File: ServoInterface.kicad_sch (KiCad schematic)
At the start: 7 parts, among them J10 ServoInputSW, J11 ServoOut

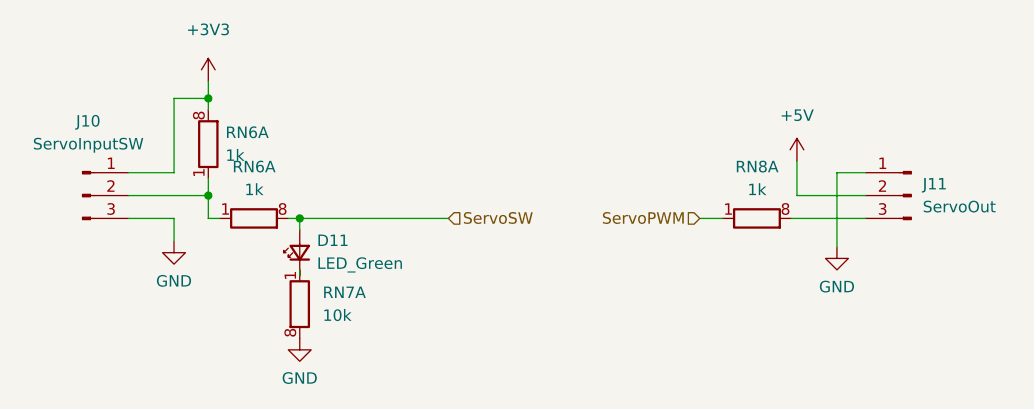
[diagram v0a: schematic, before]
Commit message: Silkscreen updates
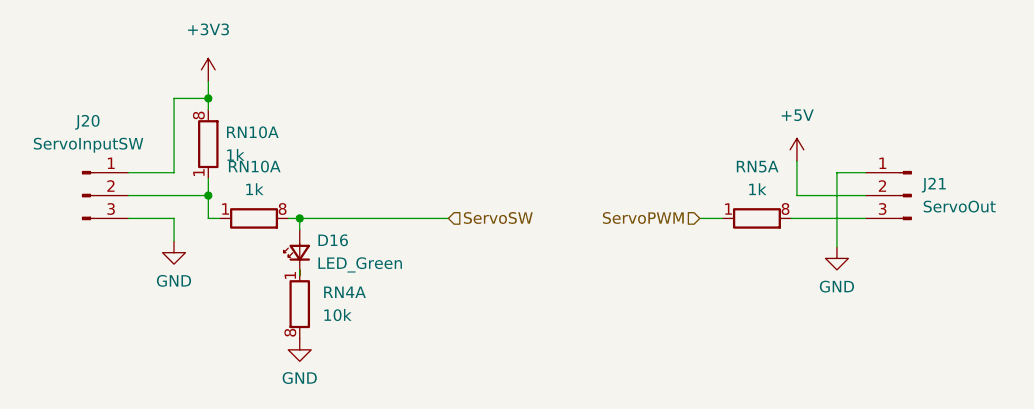
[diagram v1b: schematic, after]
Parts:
- renumbered D11 to D16, J10 to J20, J11 to J21, RN6 to RN10, RN7 to RN4, RN8 to RN5
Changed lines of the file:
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@@
   (symbol (lib_id "power:GND") (at 95.885 83.185 0)
     (in_bom yes) (on_board yes) (fields_autoplaced)
-    (property "Reference" "#PWR059" (id 0) (at 95.885 89.535 0)
+    (property "Reference" "#PWR061" (id 0) (at 95.885 89.535 0)
       (effects (font (size 1.27 1.27)) hide)
     )
@@
   (symbol (lib_id "Device:R_Pack04_Split") (at 160.655 80.645 270)
     (in_bom yes) (on_board yes) (fields_autoplaced)
-    (property "Reference" "RN8" (id 0) (at 160.655 74.93 90))
+    (property "Reference" "RN5" (id 0) (at 160.655 74.93 90))
     (property "Value" "1k" (id 1) (at 160.655 77.47 90))
     (property "Footprint" "Resistor_SMD:R_Array_Convex_4x0603" (id 2) (at 160.655 78.613 90)
@@
       (effects (font (size 1.27 1.27)) hide)
     )
-    (pin "1")
-    (pin "8")
+    (pin "2")
+    (pin "7")
   )
   (symbol (lib_id "Device:R_Pack04_Split") (at 99.695 72.39 0)
     (in_bom yes) (on_board yes) (fields_autoplaced)
-    (property "Reference" "RN6" (id 0) (at 101.6 71.1199 0)
+    (property "Reference" "RN10" (id 0) (at 101.6 71.1199 0)
       (effects (font (size 1.27 1.27)) (justify left))
     )
@@
       (effects (font (size 1.27 1.27)) hide)
     )
-    (pin "2")
-    (pin "7")
+    (pin "3")
+    (pin "6")
   )
   (symbol (lib_id "Connector:Conn_01x03_Male") (at 85.725 78.105 0)
     (in_bom yes) (on_board yes) (fields_autoplaced)
-    (property "Reference" "J10" (id 0) (at 86.36 69.85 0))
+    (property "Reference" "J20" (id 0) (at 86.36 69.85 0))
     (property "Value" "ServoInputSW" (id 1) (at 86.36 72.39 0))
     (property "Footprint" "Connector_PinHeader_2.54mm:PinHeader_1x03_P2.54mm_Vertical" (id 2) (at 85.725 78.105 0)
@@
   (symbol (lib_id "power:+3V3") (at 99.695 65.405 0)
     (in_bom yes) (on_board yes) (fields_autoplaced)
-    (property "Reference" "#PWR060" (id 0) (at 99.695 69.215 0)
+    (property "Reference" "#PWR062" (id 0) (at 99.695 69.215 0)
       (effects (font (size 1.27 1.27)) hide)
     )
@@
   (symbol (lib_id "Connector:Conn_01x03_Male") (at 177.8 78.105 0) (mirror y)
     (in_bom yes) (on_board yes) (fields_autoplaced)
-    (property "Reference" "J11" (id 0) (at 179.07 76.8349 0)
+    (property "Reference" "J21" (id 0) (at 179.07 76.8349 0)
       (effects (font (size 1.27 1.27)) (justify right))
     )
@@
   (symbol (lib_id "Device:R_Pack04_Split") (at 109.855 90.17 180)
     (in_bom yes) (on_board yes) (fields_autoplaced)
-    (property "Reference" "RN7" (id 0) (at 112.395 88.8999 0)
+    (property "Reference" "RN4" (id 0) (at 112.395 88.8999 0)
       (effects (font (size 1.27 1.27)) (justify right))
     )
@@
       (effects (font (size 1.27 1.27)) hide)
     )
-    (pin "1")
-    (pin "8")
+    (pin "2")
+    (pin "7")
   )
   (symbol (lib_id "Device:LED_Small") (at 109.855 84.455 90)
     (in_bom yes) (on_board yes) (fields_autoplaced)
-    (property "Reference" "D11" (id 0) (at 111.76 83.1214 90)
+    (property "Reference" "D16" (id 0) (at 111.76 83.1214 90)
       (effects (font (size 1.27 1.27)) (justify right))
     )
@@
   (symbol (lib_id "power:+5V") (at 165.1 74.295 0)
     (in_bom yes) (on_board yes) (fields_autoplaced)
-    (property "Reference" "#PWR062" (id 0) (at 165.1 78.105 0)
+    (property "Reference" "#PWR064" (id 0) (at 165.1 78.105 0)
       (effects (font (size 1.27 1.27)) hide)
     )
@@
   (symbol (lib_id "Device:R_Pack04_Split") (at 104.775 80.645 270)
     (in_bom yes) (on_board yes) (fields_autoplaced)
-    (property "Reference" "RN6" (id 0) (at 104.775 74.93 90))
+    (property "Reference" "RN10" (id 0) (at 104.775 74.93 90))
     (property "Value" "1k" (id 1) (at 104.775 77.47 90))
     (property "Footprint" "Resistor_SMD:R_Array_Convex_4x0603" (id 2) (at 104.775 78.613 90)
@@
       (effects (font (size 1.27 1.27)) hide)
     )
-    (pin "1")
-    (pin "8")
+    (pin "4")
+    (pin "5")
   )
   (symbol (lib_id "power:GND") (at 109.855 93.98 0)
     (in_bom yes) (on_board yes) (fields_autoplaced)
-    (property "Reference" "#PWR061" (id 0) (at 109.855 100.33 0)
+    (property "Reference" "#PWR063" (id 0) (at 109.855 100.33 0)
       (effects (font (size 1.27 1.27)) hide)
     )
@@
   (symbol (lib_id "power:GND") (at 169.545 83.82 0)
     (in_bom yes) (on_board yes) (fields_autoplaced)
-    (property "Reference" "#PWR063" (id 0) (at 169.545 90.17 0)
+    (property "Reference" "#PWR065" (id 0) (at 169.545 90.17 0)
       (effects (font (size 1.27 1.27)) hide)
     )

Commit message: Add licence
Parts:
- renumbered D16 to D13, J20 to J14, J21 to J15, RN4 to RN7, RN5 to RN8, RN10 to RN9
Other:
- company: (none) -> AntTronics
- title: (none) -> ServoSwitch
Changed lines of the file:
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@@
 (kicad_sch (version 20211123) (generator eeschema)
   (paper "A4")
+  (title_block
+    (title "ServoSwitch")
+    (date "2023-12-20")
+    (rev "0.1")
+    (company "AntTronics")
+  )
   (junction (at 99.695 67.31) (diameter 0) (color 0 0 0 0)
   )
@@
   (symbol (lib_id "power:GND") (at 95.885 83.185 0)
     (in_bom yes) (on_board yes) (fields_autoplaced)
-    (property "Reference" "#PWR061" (id 0) (at 95.885 89.535 0)
+    (property "Reference" "#PWR046" (id 0) (at 95.885 89.535 0)
       (effects (font (size 1.27 1.27)) hide)
     )
@@
   (symbol (lib_id "Device:R_Pack04_Split") (at 160.655 80.645 270)
     (in_bom yes) (on_board yes) (fields_autoplaced)
-    (property "Reference" "RN5" (id 0) (at 160.655 74.93 90))
+    (property "Reference" "RN8" (id 0) (at 160.655 74.93 90))
     (property "Value" "1k" (id 1) (at 160.655 77.47 90))
     (property "Footprint" "Resistor_SMD:R_Array_Convex_4x0603" (id 2) (at 160.655 78.613 90)
@@
       (effects (font (size 1.27 1.27)) hide)
     )
-    (pin "2")
-    (pin "7")
+    (pin "3")
+    (pin "6")
   )
   (symbol (lib_id "Device:R_Pack04_Split") (at 99.695 72.39 0)
     (in_bom yes) (on_board yes) (fields_autoplaced)
-    (property "Reference" "RN10" (id 0) (at 101.6 71.1199 0)
+    (property "Reference" "RN9" (id 0) (at 101.6 71.1199 0)
       (effects (font (size 1.27 1.27)) (justify left))
     )
@@
       (effects (font (size 1.27 1.27)) hide)
     )
-    (pin "3")
-    (pin "6")
+    (pin "2")
+    (pin "7")
   )
   (symbol (lib_id "Connector:Conn_01x03_Male") (at 85.725 78.105 0)
     (in_bom yes) (on_board yes) (fields_autoplaced)
-    (property "Reference" "J20" (id 0) (at 86.36 69.85 0))
+    (property "Reference" "J14" (id 0) (at 86.36 69.85 0))
     (property "Value" "ServoInputSW" (id 1) (at 86.36 72.39 0))
     (property "Footprint" "Connector_PinHeader_2.54mm:PinHeader_1x03_P2.54mm_Vertical" (id 2) (at 85.725 78.105 0)
@@
   (symbol (lib_id "power:+3V3") (at 99.695 65.405 0)
     (in_bom yes) (on_board yes) (fields_autoplaced)
-    (property "Reference" "#PWR062" (id 0) (at 99.695 69.215 0)
+    (property "Reference" "#PWR047" (id 0) (at 99.695 69.215 0)
       (effects (font (size 1.27 1.27)) hide)
     )
@@
   (symbol (lib_id "Connector:Conn_01x03_Male") (at 177.8 78.105 0) (mirror y)
     (in_bom yes) (on_board yes) (fields_autoplaced)
-    (property "Reference" "J21" (id 0) (at 179.07 76.8349 0)
+    (property "Reference" "J15" (id 0) (at 179.07 76.8349 0)
       (effects (font (size 1.27 1.27)) (justify right))
     )
@@
   (symbol (lib_id "Device:R_Pack04_Split") (at 109.855 90.17 180)
     (in_bom yes) (on_board yes) (fields_autoplaced)
-    (property "Reference" "RN4" (id 0) (at 112.395 88.8999 0)
+    (property "Reference" "RN7" (id 0) (at 112.395 88.8999 0)
       (effects (font (size 1.27 1.27)) (justify right))
     )
@@
       (effects (font (size 1.27 1.27)) hide)
     )
-    (pin "2")
-    (pin "7")
+    (pin "3")
+    (pin "6")
   )
   (symbol (lib_id "Device:LED_Small") (at 109.855 84.455 90)
     (in_bom yes) (on_board yes) (fields_autoplaced)
-    (property "Reference" "D16" (id 0) (at 111.76 83.1214 90)
+    (property "Reference" "D13" (id 0) (at 111.76 83.1214 90)
       (effects (font (size 1.27 1.27)) (justify right))
     )
@@
   (symbol (lib_id "power:+5V") (at 165.1 74.295 0)
     (in_bom yes) (on_board yes) (fields_autoplaced)
-    (property "Reference" "#PWR064" (id 0) (at 165.1 78.105 0)
+    (property "Reference" "#PWR049" (id 0) (at 165.1 78.105 0)
       (effects (font (size 1.27 1.27)) hide)
     )
@@
   (symbol (lib_id "Device:R_Pack04_Split") (at 104.775 80.645 270)
     (in_bom yes) (on_board yes) (fields_autoplaced)
-    (property "Reference" "RN10" (id 0) (at 104.775 74.93 90))
+    (property "Reference" "RN9" (id 0) (at 104.775 74.93 90))
     (property "Value" "1k" (id 1) (at 104.775 77.47 90))
     (property "Footprint" "Resistor_SMD:R_Array_Convex_4x0603" (id 2) (at 104.775 78.613 90)
@@
       (effects (font (size 1.27 1.27)) hide)
     )
-    (pin "4")
-    (pin "5")
+    (pin "1")
+    (pin "8")
   )
   (symbol (lib_id "power:GND") (at 109.855 93.98 0)
     (in_bom yes) (on_board yes) (fields_autoplaced)
-    (property "Reference" "#PWR063" (id 0) (at 109.855 100.33 0)
+    (property "Reference" "#PWR048" (id 0) (at 109.855 100.33 0)
       (effects (font (size 1.27 1.27)) hide)
     )
@@
   (symbol (lib_id "power:GND") (at 169.545 83.82 0)
     (in_bom yes) (on_board yes) (fields_autoplaced)
-    (property "Reference" "#PWR065" (id 0) (at 169.545 90.17 0)
-      (effects (font (size 1.27 1.27)) hide)
-    )
+    (property "Reference" "#PWR050" (id 0) (at 169.545 90.17 0)
+      (effects (font (size 1.27 1.27)) hide)
+    )
